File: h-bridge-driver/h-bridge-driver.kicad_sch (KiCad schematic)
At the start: 25 parts, among them J1 CON_HDR_100MILS_M_TH_2X8, J2 CON_TERM_BLK_1X2_TB008A-508-0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, Q1 TRX_NMOS_PJD40N04_L2_00001, Q2 TRX_NMOS_PJD40N04_L2_00001, Q3 TRX_NMOS_PJD40N04_L2_00001, Q4 TRX_NMOS_PJD40N04_L2_00001, U1 DRV_A4957SESTR-T

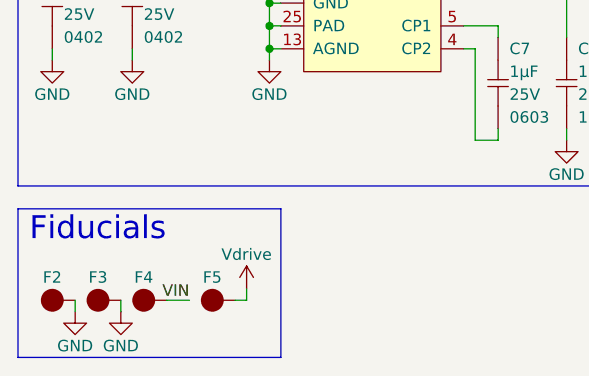
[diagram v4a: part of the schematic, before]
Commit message: rename project, comple simple switch layout, fix thermal reliefs
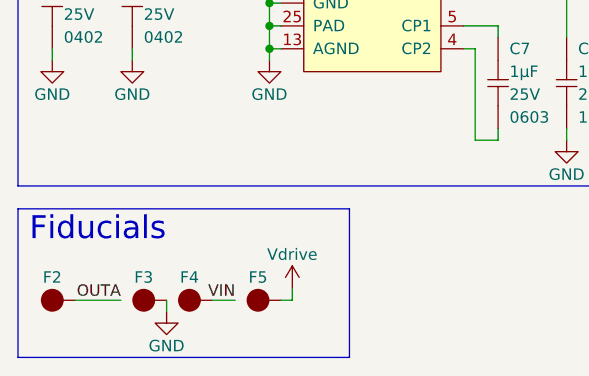
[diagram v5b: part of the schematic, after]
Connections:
- net GND: no longer F2.1
- net OUTA: now also F2.1
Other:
- moved on the sheet: F3, F4, F5
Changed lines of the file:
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@@
     (stroke (width 0) (type default) (color 0 0 0 0))
   )
-  (polyline (pts (xy 44.45 158.75) (xy 44.45 142.24))
+  (polyline (pts (xy 52.07 158.75) (xy 52.07 142.24))
     (stroke (width 0) (type default) (color 0 0 0 0))
   )
@@
     (stroke (width 0) (type default) (color 0 0 0 0))
   )
-  (wire (pts (xy 39.37 152.4) (xy 40.64 152.4))
+  (wire (pts (xy 44.45 152.4) (xy 45.72 152.4))
     (stroke (width 0) (type default) (color 0 0 0 0))
   )
@@
     (stroke (width 0) (type default) (color 0 0 0 0))
   )
+  (wire (pts (xy 21.59 152.4) (xy 26.67 152.4))
+    (stroke (width 0) (type default) (color 0 0 0 0))
+  )
   (polyline (pts (xy 134.62 60.96) (xy 134.62 139.7))
     (stroke (width 0) (type default) (color 0 0 0 0))
@@
     (stroke (width 0) (type default) (color 0 0 0 0))
   )
-  (wire (pts (xy 21.59 152.4) (xy 21.59 153.67))
-    (stroke (width 0) (type default) (color 0 0 0 0))
-  )
-  (wire (pts (xy 26.67 152.4) (xy 26.67 153.67))
+  (wire (pts (xy 31.75 152.4) (xy 31.75 153.67))
     (stroke (width 0) (type default) (color 0 0 0 0))
   )
@@
     (stroke (width 0) (type default) (color 0 0 0 0))
   )
-  (polyline (pts (xy 15.24 142.24) (xy 44.45 142.24))
+  (polyline (pts (xy 15.24 142.24) (xy 52.07 142.24))
     (stroke (width 0) (type default) (color 0 0 0 0))
   )
@@
     (stroke (width 0) (type default) (color 0 0 0 0))
   )
-  (wire (pts (xy 40.64 152.4) (xy 40.64 151.13))
+  (wire (pts (xy 45.72 152.4) (xy 45.72 151.13))
     (stroke (width 0) (type default) (color 0 0 0 0))
   )
@@
     (stroke (width 0) (type default) (color 0 0 0 0))
   )
-  (wire (pts (xy 31.75 152.4) (xy 34.29 152.4))
+  (wire (pts (xy 36.83 152.4) (xy 39.37 152.4))
     (stroke (width 0) (type default) (color 0 0 0 0))
   )
@@
     (stroke (width 0) (type default) (color 0 0 0 0))
   )
-  (polyline (pts (xy 15.24 158.75) (xy 44.45 158.75))
+  (polyline (pts (xy 15.24 158.75) (xy 52.07 158.75))
     (stroke (width 0) (type default) (color 0 0 0 0))
   )
@@
     (effects (font (size 1.27 1.27)) (justify left bottom))
   )
-  (label "VIN" (at 34.29 152.4 180)
+  (label "VIN" (at 39.37 152.4 180)
     (effects (font (size 1.27 1.27)) (justify right bottom))
   )
@@
   (label "RST" (at 29.21 99.06 0)
     (effects (font (size 1.27 1.27)) (justify left bottom))
+  )
+  (label "OUTA" (at 26.67 152.4 180)
+    (effects (font (size 1.27 1.27)) (justify right bottom))
   )
   (symbol (lib_id "connaxio-connectors:FUS_BLADE_MINI_3588-1") (at 60.96 54.61 0) (unit 1)
@@
     (pin "3")
   )
-  (symbol (lib_name "FID_1X1_3") (lib_id "connaxio-mechanical:FID_1X1") (at 36.83 152.4 0) (unit 1)
+  (symbol (lib_name "FID_1X1_3") (lib_id "connaxio-mechanical:FID_1X1") (at 41.91 152.4 0) (unit 1)
     (in_bom no) (on_board yes)
-    (property "Reference" "F5" (id 0) (at 36.83 149.86 0))
-    (property "Value" "FID_1X1" (id 1) (at 39.624 145.923 0)
-      (effects (font (size 1.27 1.27)) hide)
-    )
-    (property "Footprint" "connaxio-mechanical:FID_1X1" (id 2) (at 48.1076 140.3096 0)
-      (effects (font (size 1.27 1.27)) hide)
-    )
-    (property "Datasheet" "" (id 3) (at 36.83 152.4 0)
+    (property "Reference" "F5" (id 0) (at 41.91 149.86 0))
+    (property "Value" "FID_1X1" (id 1) (at 44.704 145.923 0)
+      (effects (font (size 1.27 1.27)) hide)
+    )
+    (property "Footprint" "connaxio-mechanical:FID_1X1" (id 2) (at 53.1876 140.3096 0)
+      (effects (font (size 1.27 1.27)) hide)
+    )
+    (property "Datasheet" "" (id 3) (at 41.91 152.4 0)
       (effects (font (size 1.27 1.27)) hide)
     )
@@
     (pin "1")
   )
-  (symbol (lib_name "FID_1X1_2") (lib_id "connaxio-mechanical:FID_1X1") (at 29.21 152.4 0) (unit 1)
+  (symbol (lib_name "FID_1X1_2") (lib_id "connaxio-mechanical:FID_1X1") (at 34.29 152.4 0) (unit 1)
     (in_bom no) (on_board yes)
-    (property "Reference" "F4" (id 0) (at 29.21 149.86 0))
-    (property "Value" "FID_1X1" (id 1) (at 32.004 145.923 0)
-      (effects (font (size 1.27 1.27)) hide)
-    )
-    (property "Footprint" "connaxio-mechanical:FID_1X1" (id 2) (at 40.4876 140.3096 0)
-      (effects (font (size 1.27 1.27)) hide)
-    )
-    (property "Datasheet" "" (id 3) (at 29.21 152.4 0)
+    (property "Reference" "F4" (id 0) (at 34.29 149.86 0))
+    (property "Value" "FID_1X1" (id 1) (at 37.084 145.923 0)
+      (effects (font (size 1.27 1.27)) hide)
+    )
+    (property "Footprint" "connaxio-mechanical:FID_1X1" (id 2) (at 45.5676 140.3096 0)
+      (effects (font (size 1.27 1.27)) hide)
+    )
+    (property "Datasheet" "" (id 3) (at 34.29 152.4 0)
       (effects (font (size 1.27 1.27)) hide)
     )
@@
     (pin "2")
   )
-  (symbol (lib_id "power:Vdrive") (at 40.64 151.13 0) (unit 1)
-    (in_bom yes) (on_board yes)
-    (property "Reference" "#PWR017" (id 0) (at 35.56 154.94 0)
-      (effects (font (size 1.27 1.27)) hide)
-    )
-    (property "Value" "Vdrive" (id 1) (at 40.64 147.32 0))
-    (property "Footprint" "" (id 2) (at 40.64 151.13 0)
-      (effects (font (size 1.27 1.27)) hide)
-    )
-    (property "Datasheet" "" (id 3) (at 40.64 151.13 0)
+  (symbol (lib_id "power:Vdrive") (at 45.72 151.13 0) (unit 1)
+    (in_bom yes) (on_board yes)
+    (property "Reference" "#PWR017" (id 0) (at 40.64 154.94 0)
+      (effects (font (size 1.27 1.27)) hide)
+    )
+    (property "Value" "Vdrive" (id 1) (at 45.72 147.32 0))
+    (property "Footprint" "" (id 2) (at 45.72 151.13 0)
+      (effects (font (size 1.27 1.27)) hide)
+    )
+    (property "Datasheet" "" (id 3) (at 45.72 151.13 0)
       (effects (font (size 1.27 1.27)) hide)
     )
@@
     (pin "2")
   )
-  (symbol (lib_id "power:GND") (at 21.59 153.67 0) (unit 1)
-    (in_bom yes) (on_board yes)
-    (property "Reference" "#PWR018" (id 0) (at 21.59 160.02 0)
-      (effects (font (size 1.27 1.27)) hide)
-    )
-    (property "Value" "GND" (id 1) (at 21.59 157.48 0))
-    (property "Footprint" "" (id 2) (at 21.59 153.67 0)
-      (effects (font (size 1.27 1.27)) hide)
-    )
-    (property "Datasheet" "" (id 3) (at 21.59 153.67 0)
-      (effects (font (size 1.27 1.27)) hide)
-    )
-    (pin "1")
-  )
   (symbol (lib_id "connaxio-capacitors:CAP_CER_10UF_25V_1206") (at 76.2 128.27 0) (unit 1)
     (in_bom yes) (on_board yes)
@@
     (pin "2")
   )
-  (symbol (lib_id "power:GND") (at 26.67 153.67 0) (unit 1)
-    (in_bom yes) (on_board yes)
-    (property "Reference" "#PWR019" (id 0) (at 26.67 160.02 0)
-      (effects (font (size 1.27 1.27)) hide)
-    )
-    (property "Value" "GND" (id 1) (at 26.67 157.48 0))
-    (property "Footprint" "" (id 2) (at 26.67 153.67 0)
-      (effects (font (size 1.27 1.27)) hide)
-    )
-    (property "Datasheet" "" (id 3) (at 26.67 153.67 0)
+  (symbol (lib_id "power:GND") (at 31.75 153.67 0) (unit 1)
+    (in_bom yes) (on_board yes)
+    (property "Reference" "#PWR019" (id 0) (at 31.75 160.02 0)
+      (effects (font (size 1.27 1.27)) hide)
+    )
+    (property "Value" "GND" (id 1) (at 31.75 157.48 0))
+    (property "Footprint" "" (id 2) (at 31.75 153.67 0)
+      (effects (font (size 1.27 1.27)) hide)
+    )
+    (property "Datasheet" "" (id 3) (at 31.75 153.67 0)
       (effects (font (size 1.27 1.27)) hide)
     )
@@
     (pin "2")
   )
-  (symbol (lib_name "FID_1X1_1") (lib_id "connaxio-mechanical:FID_1X1") (at 24.13 152.4 0) (unit 1)
+  (symbol (lib_name "FID_1X1_1") (lib_id "connaxio-mechanical:FID_1X1") (at 29.21 152.4 0) (unit 1)
     (in_bom no) (on_board yes)
-    (property "Reference" "F3" (id 0) (at 24.13 149.86 0))
-    (property "Value" "FID_1X1" (id 1) (at 26.924 145.923 0)
-      (effects (font (size 1.27 1.27)) hide)
-    )
-    (property "Footprint" "connaxio-mechanical:FID_1X1" (id 2) (at 35.4076 140.3096 0)
-      (effects (font (size 1.27 1.27)) hide)
-    )
-    (property "Datasheet" "" (id 3) (at 24.13 152.4 0)
+    (property "Reference" "F3" (id 0) (at 29.21 149.86 0))
+    (property "Value" "FID_1X1" (id 1) (at 32.004 145.923 0)
+      (effects (font (size 1.27 1.27)) hide)
+    )
+    (property "Footprint" "connaxio-mechanical:FID_1X1" (id 2) (at 40.4876 140.3096 0)
+      (effects (font (size 1.27 1.27)) hide)
+    )
+    (property "Datasheet" "" (id 3) (at 29.21 152.4 0)
       (effects (font (size 1.27 1.27)) hide)
     )
@@
       (reference "#PWR017") (unit 1) (value "Vdrive") (footprint "")
     )
-    (path "/6ea4e2d4-b316-4235-ba3f-cbfb7b06b57f"
-      (reference "#PWR018") (unit 1) (value "GND") (footprint "")
-    )
     (path "/d771fa67-d50f-4301-b6d0-028327c3d2ef"

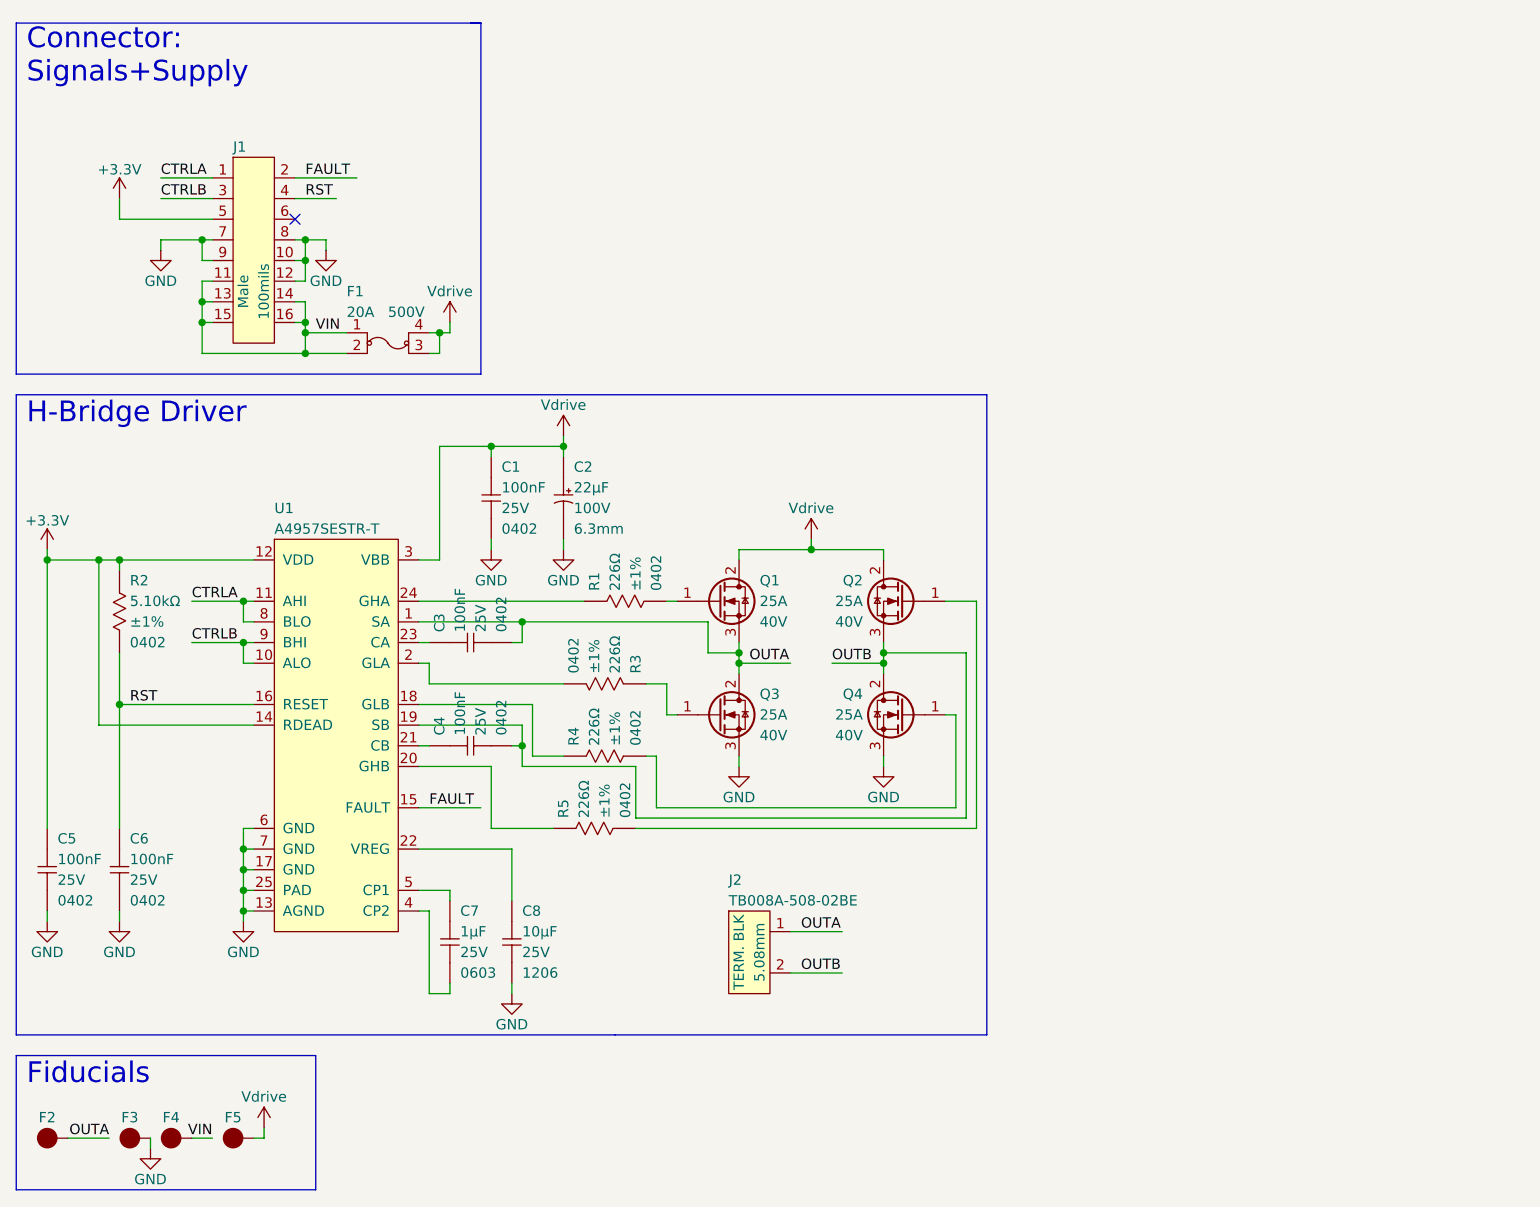
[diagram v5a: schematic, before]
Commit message: Inverted motor controls for open-drain operation and manual switch override compatibility
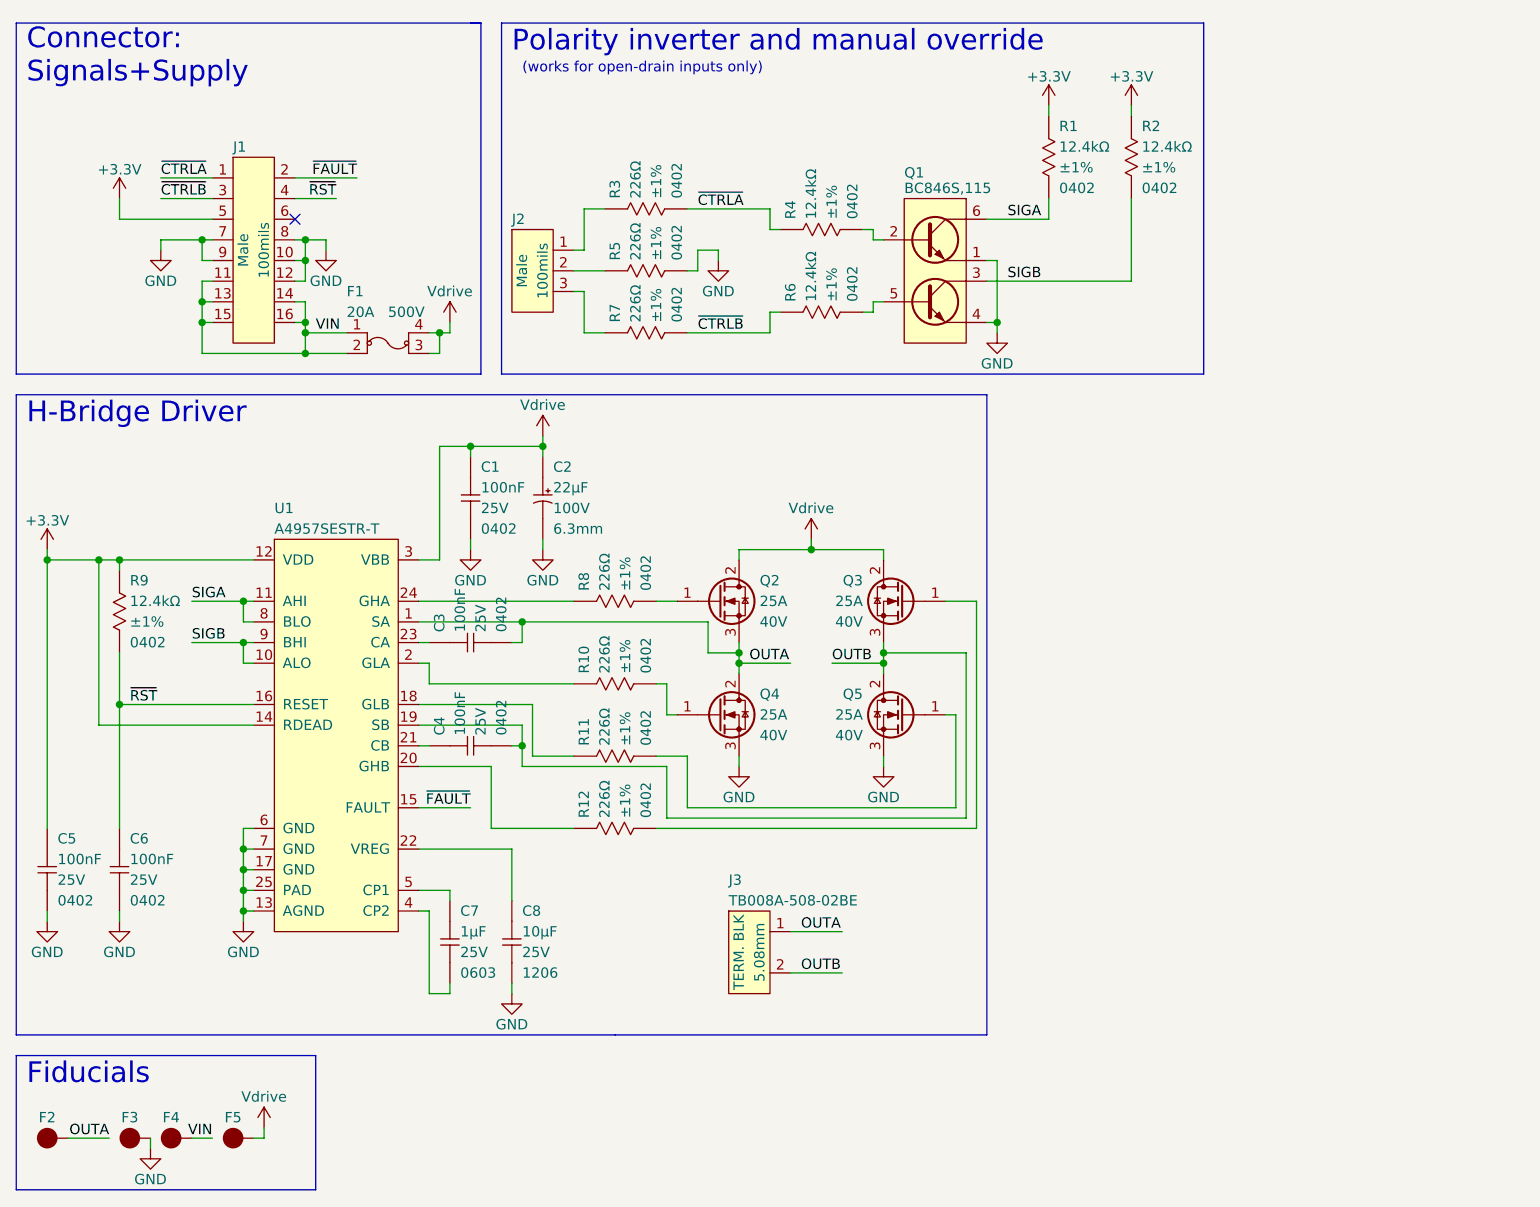
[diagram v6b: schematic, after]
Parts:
- removed R2: RES_5.10KΩ_1%_0402, connaxio-resistors:RES_0402_1005M, symbol connaxio-resistors:RES_5.10KΩ_1%_0402
- added J2: CON_HDR_100MILS_M_TH_1X3, connaxio-connectors:CON_HDR_100MILS_M_TH_1X3, symbol connaxio-connectors:CON_HDR_100MILS_M_TH_1X3
- added Q1: TRX_2NPN_BC846S,115, connaxio-sop:SOT-363_SC-70-6, symbol connaxio-transistors:TRX_2NPN_BC846S,115
- added R1, R2, R4, R6, R9: RES_12.4KΩ_1%_0402, connaxio-resistors:RES_0402_1005M, symbol connaxio-resistors:RES_12.4KΩ_1%_0402
- added R3, R5, R7: RES_226Ω_1%_0402, connaxio-resistors:RES_0402_1005M, symbol connaxio-resistors:RES_226Ω_1%_0402
- renumbered J2 to J3, Q1 to Q2, Q2 to Q3, Q3 to Q4, Q4 to Q5, R3 to R10, R4 to R11, R5 to R12, R1 to R8
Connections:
- net +3.3V: now also R1.1, R2.1, R9.1
- net GND: now also Q1.1 (E1), Q1.4 (E2), R5.2
- net at Q4.1 (G): now also R10.2; no longer R10.1
- net at U1.2 (GLA): now also R10.1; no longer R10.2
- net CTRLA renamed SIGA
- net SIGA: now also Q1.6 (C1), R1.2; no longer J1.1
- net CTRLB renamed SIGB
- net SIGB: now also Q1.3 (C2), R2.2; no longer J1.3
- net FAULT renamed ~{FAULT}
- net RST renamed ~{RST}
- net ~{RST}: now also R9.2
- new net: Q1.2 (B1), R4.2
- new net: J2.1, R3.1
- new net: Q1.5 (B2), R6.2
- new net: J2.3, R7.1
- new net: J2.2, R5.1
- new net ~{CTRLA}: J1.1, R3.2, R4.1
- new net ~{CTRLB}: J1.3, R6.1, R7.2
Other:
- note added: "(works for open-drain inputs only)"
- note added: "Polarity inverter and manual override"
- moved on the sheet: C1, C2, R10, R11, R12, R8
